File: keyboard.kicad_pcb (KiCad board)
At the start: 2 copper layers, 74 parts, among them CON1 USB-MICRO-B, J1 CONN-PALM-FOLD-KB, P1 Keyboard Even, P2 Keyboard Odd, P3 PS2, P4 Palm Serial, P5 ARM debug header, Q1 BSS138, Q2 BSS138, Q3 BSS138, SW1 SW_PUSH, U1 CONN-X220-KB, U2 MCP1700-2202E/TT, U3 EFM32G222F32, X1 CRYSTAL

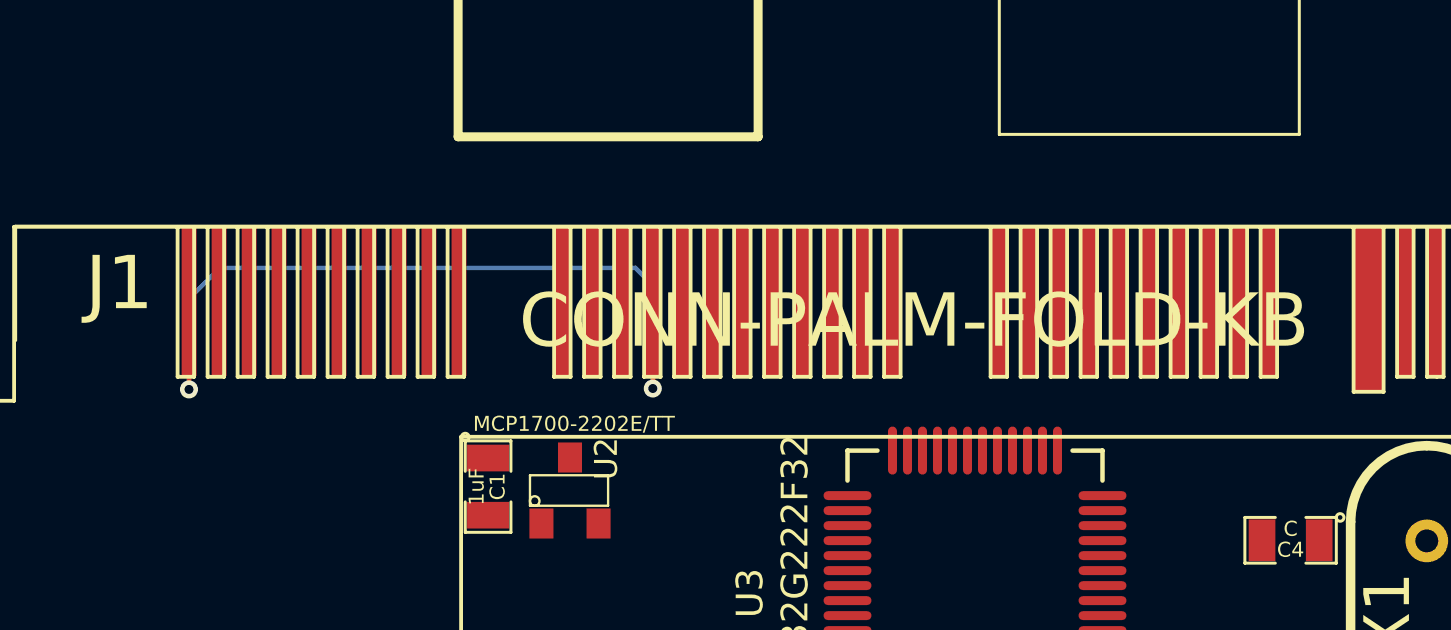
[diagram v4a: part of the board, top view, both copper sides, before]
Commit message: First pass at joining up the duplicated palm connections
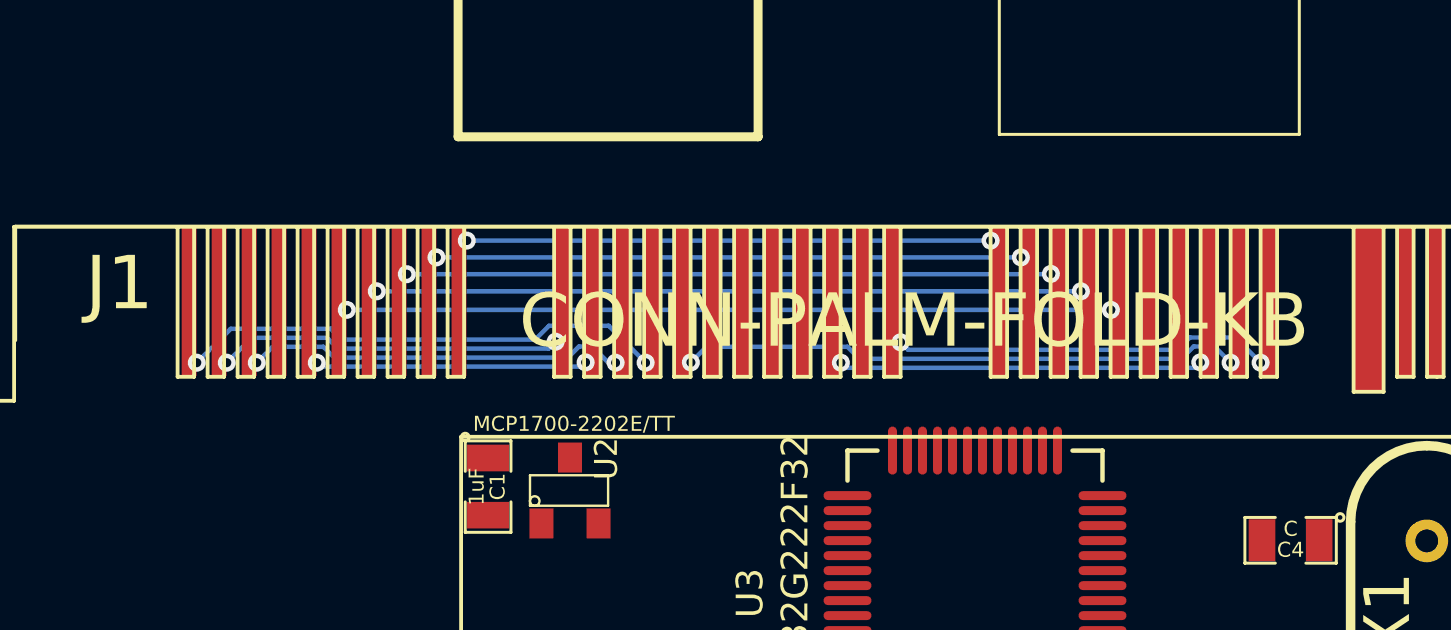
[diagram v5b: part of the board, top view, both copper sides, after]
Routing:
- net row8: track 0.00 -> 26.3 mm, vias 0 -> 2
- net col12: track 0.00 -> 24.3 mm, vias 0 -> 2
- net row7: track 0.00 -> 23.5 mm, vias 0 -> 2
- net col5: track 0.00 -> 23.1 mm, vias 0 -> 2
- net row6: track 0.00 -> 22.6 mm, vias 0 -> 2
- net row5: track 0.00 -> 21.7 mm, vias 0 -> 2
- net col8: track 0.00 -> 17.0 mm, vias 0 -> 2
- net col6: track 0.00 -> 16.4 mm, vias 0 -> 2
- net col1: track 0.00 -> 16.3 mm, vias 0 -> 2
- net col10: track 0.00 -> 15.2 mm, vias 0 -> 2
- net col9: track 0.00 -> 13.4 mm, vias 0 -> 2
- net col7: track 28.5 -> 20.6 mm

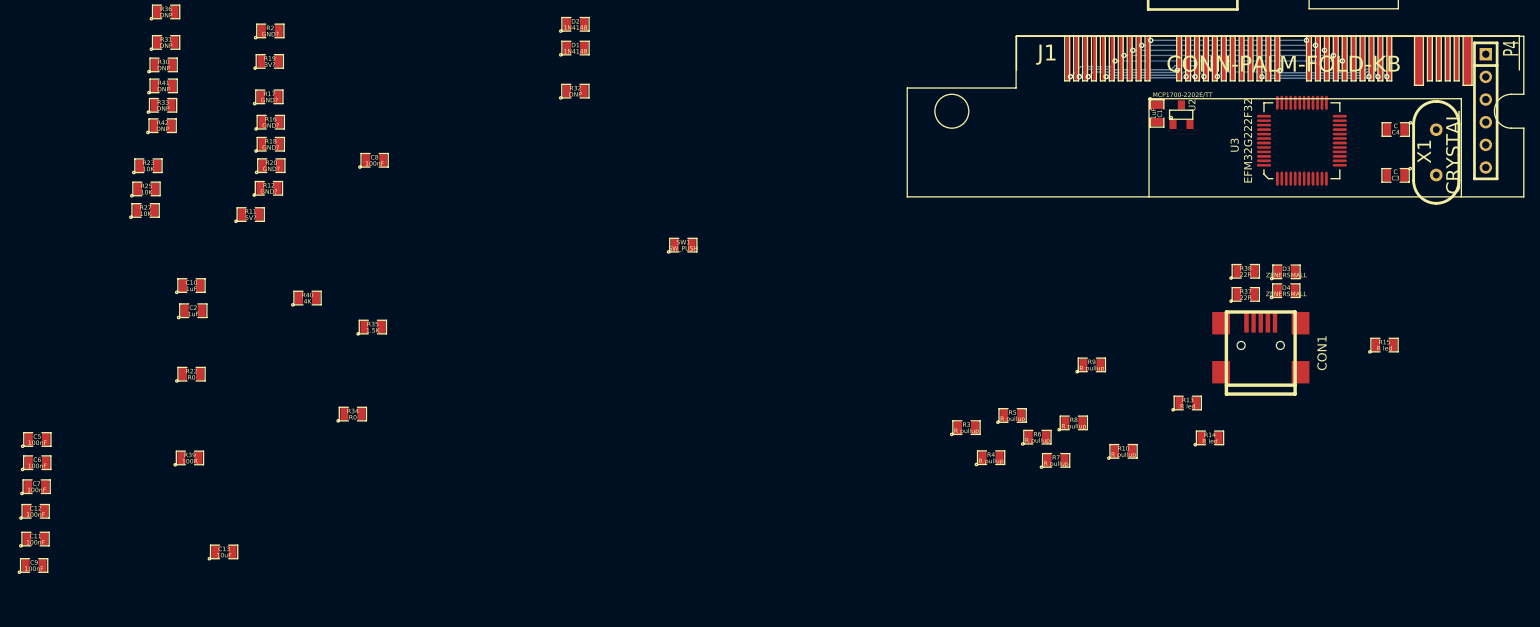
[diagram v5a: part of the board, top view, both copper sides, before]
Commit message: Route most of the palm board, ensuring that there was also enough escape for the rest of the board
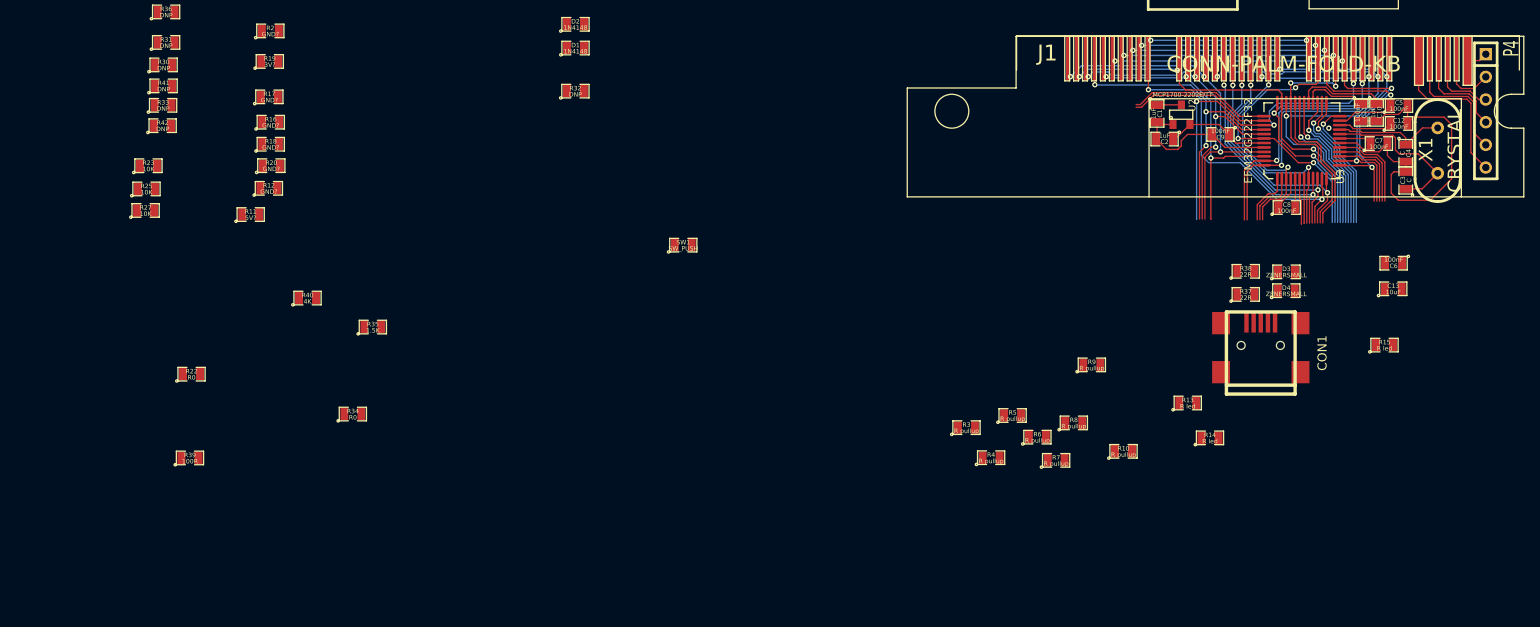
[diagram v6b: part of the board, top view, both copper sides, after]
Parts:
- moved C12 158.9 mm to (185.1, 52.8)
- moved C5 157.1 mm to (185.1, 50.8)
- moved C11 156.1 mm to (180.9, 51.5), turned to 270 degrees
- moved C7 155.3 mm to (182.9, 55.0)
- moved C6 153.6 mm to (184.5, 68.4), turned to 180 degrees
- moved C9 141.5 mm to (165.1, 54.0), turned to 180 degrees
- moved C13 134.3 mm to (184.5, 71.3)
- moved C10 134.2 mm to (182.6, 51.5), turned to 270 degrees
- moved C2 110.5 mm to (158.8, 54.5), turned to 180 degrees
- moved C8 102.4 mm to (172.5, 62.2)
- moved C4 2.88 mm to (185.9, 56.1), turned to 270 degrees
- moved C3 1.27 mm to (185.9, 59.1), turned to 90 degrees
- moved X1 0.26 mm to (189.4, 55.8)
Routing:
- net GND: track 0.00 -> 63.8 mm
- net col11: track 0.00 -> 39.3 mm, vias 0 -> 3
- net +3.3V: track 0.00 -> 39.2 mm
- net row5: track 21.7 -> 58.8 mm, vias 2 -> 4
- net col3: track 0.00 -> 37.1 mm, vias 0 -> 3
- net col10: track 15.2 -> 48.2 mm, vias 2 -> 3
- net col2: track 0.00 -> 32.8 mm, vias 0 -> 3
- net col1: track 16.3 -> 47.0 mm, vias 2 -> 3
- net row6: track 22.6 -> 52.8 mm, vias 2 -> 4
- net col5: track 23.1 -> 51.9 mm, vias 2 -> 3
- net row2: track 0.00 -> 28.6 mm, vias 0 -> 2
- net row7: track 23.5 -> 52.0 mm, vias 2 -> 4
- net col6: track 16.4 -> 44.7 mm, vias 2 -> 3
- net col12: track 24.3 -> 52.0 mm, vias 2 -> 4
- net col4: track 0.00 -> 27.6 mm, vias 0 -> 3
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
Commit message: Fully routed board, done with new kicad 5533
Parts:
- removed CON1: USB-MICRO-B, USB_MINI_B
- added P6: Power, Pin_Headers:Pin_Header_Straight_1x04, F.Cu at (132.7, 96.8)
- added P7: USB_H, Pin_Headers:Pin_Header_Straight_1x04, F.Cu at (140.6, 81.7)
- added REF**: DNP, Resistors_SMD:R_0805_HandSoldering, F.Cu at (196.3, 105.3)
- added USB: USB-MICRO-B, USB_MINI_B, F.Cu at (134.2, 86.5)
- R30, R31: footprint SM0805 -> Resistors_SMD:R_0805
- moved R27 151.7 mm to (196.2, 68.3)
- moved R23 147.8 mm to (192.3, 68.3)
- moved R25 143.7 mm to (188.2, 68.3)
- moved R2 137.8 mm to (189.8, 84.6)
- moved R12 134.4 mm to (189.8, 88.6)
- moved R20 134.3 mm to (189.8, 86.6)
- moved R31 133.7 mm to (163.9, 108.4), turned to 90 degrees
- moved R19 132.3 mm to (183.2, 90.3)
- moved R11 132.0 mm to (186.3, 86.6)
- moved R30 131.2 mm to (163.9, 105.2), turned to 90 degrees
- moved R18 124.5 mm to (178.2, 90.1)
- moved R36 122.0 mm to (167.0, 62.0)
- moved R22 121.1 mm to (168.2, 106.2), turned to 180 degrees
- moved R17 120.0 mm to (175.8, 75.3)
- moved R16 119.6 mm to (175.7, 77.1)
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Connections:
- C11 pad 1: +3.3V -> +3V3
- C12 pad 1: +3.3V -> +3V3
- C13 pad 1: +3.3V -> +3V3
- C2 pad 1: +3.3V -> +3V3
- C5 pad 1: +3.3V -> +3V3
- C7 pad 1: +3.3V -> +3V3
- C8 pad 1: +3.3V -> +3V3
- C9 pad 1: +3.3V -> +3V3
- D2 pad 2: +5V -> +3V3
- P3 pad 2: (no net) -> Net-(P3-Pad2)
- P5 pad 1: +3.3V -> +3V3
- P5 pad 11: (no net) -> Net-(P5-Pad11)
- P5 pad 13: (no net) -> Net-(P5-Pad13)
- P5 pad 17: (no net) -> Net-(P5-Pad17)
- P5 pad 19: (no net) -> Net-(P5-Pad19)
- P5 pad 2: (no net) -> Net-(P5-Pad2)
- P5 pad 3: (no net) -> Net-(P5-Pad3)
- P5 pad 5: (no net) -> Net-(P5-Pad5)
- Q1 pad 1: +3.3V -> +3V3
- Q2 pad 1: +3.3V -> +3V3
- Q3 pad 1: +3.3V -> +3V3
- R1 pad 1: (no net) -> ledmicmute
- R10 pad 1: +3.3V -> +3V3
- R19 pad 1: +3.3V -> +3V3
- R21 pad 2: +3.3V -> +3V3
- R24 pad 2: +3.3V -> +3V3
- R26 pad 2: +3.3V -> +3V3
- R3 pad 1: +3.3V -> +3V3
- R33 pad 2: +3.3V -> +3V3
- R36 pad 2: +3.3V -> +3V3
- R4 pad 1: +3.3V -> +3V3
- R40 pad 2: +3.3V -> +3V3
- R5 pad 1: +3.3V -> +3V3
- R6 pad 1: +3.3V -> +3V3
- R7 pad 1: +3.3V -> +3V3
- R8 pad 1: +3.3V -> +3V3
- R9 pad 1: +3.3V -> +3V3
- U2 pad 2: +3.3V -> +3V3
- U3 pad 19: +3.3V -> +3V3
- U3 pad 22: +3.3V -> +3V3
- U3 pad 23: +3.3V -> +3V3
- U3 pad 28: +3.3V -> +3V3
- U3 pad 4: +3.3V -> +3V3
- U3 pad 43: +3.3V -> +3V3
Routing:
- net GND: track 63.8 -> 648.6 mm, vias 0 -> 60
- net +3V3: track 0.00 -> 255.3 mm, vias 0 -> 10
- net +5V: track 0.00 -> 164.7 mm, vias 0 -> 6
- net pwrswitch: track 0.00 -> 120.9 mm, vias 0 -> 2
- net Net-(P2-Pad13): track 0.00 -> 112.2 mm, vias 0 -> 4
- net row6: track 52.8 -> 151.6 mm
- net hotkey: track 6.31 -> 102.8 mm
- net row1: track 26.5 -> 122.1 mm
- net row8: track 52.9 -> 144.5 mm
- net row4: track 27.0 -> 114.4 mm, vias 2 -> 4
- net row3: track 27.2 -> 112.7 mm, vias 2 -> 4
- net row5: track 58.8 -> 142.7 mm, vias 4 -> 6
- net row2: track 28.6 -> 109.8 mm, vias 2 -> 4
- net Net-(P2-Pad12): track 0.00 -> 78.3 mm, vias 0 -> 2
- net col3: track 37.1 -> 114.9 mm, vias 3 -> 4
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- added copper zone on B.Cu, net GND
- added copper zone on F.Cu, net GND
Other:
- board outline added: 69.1 x 68.1 mm
- net class Pwr added: clearance 0.2, trace_width 0.2, via_dia 0.65, via_drill 0.35
- board text added: "1"
- board text added: "10"
- board text added: "15"
- board text added: "2"
- board text added: "20"
- board text added: "25"
- board text added: "30"
- board text added: "35"
- board text added: "40"
- board text added: "5"
- board text added: "Keyboard v1"

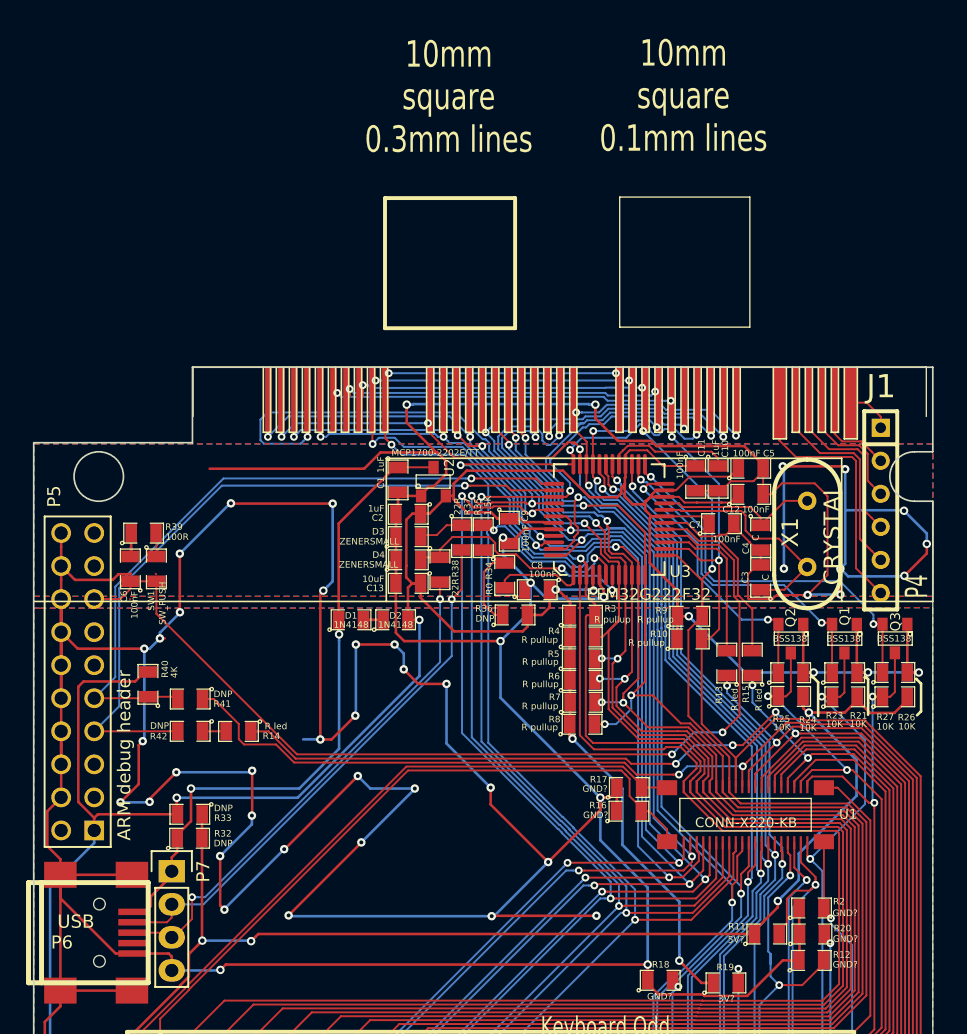
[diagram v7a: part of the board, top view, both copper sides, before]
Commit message: Tidy up silkscreen and one gnd plane misplaced via
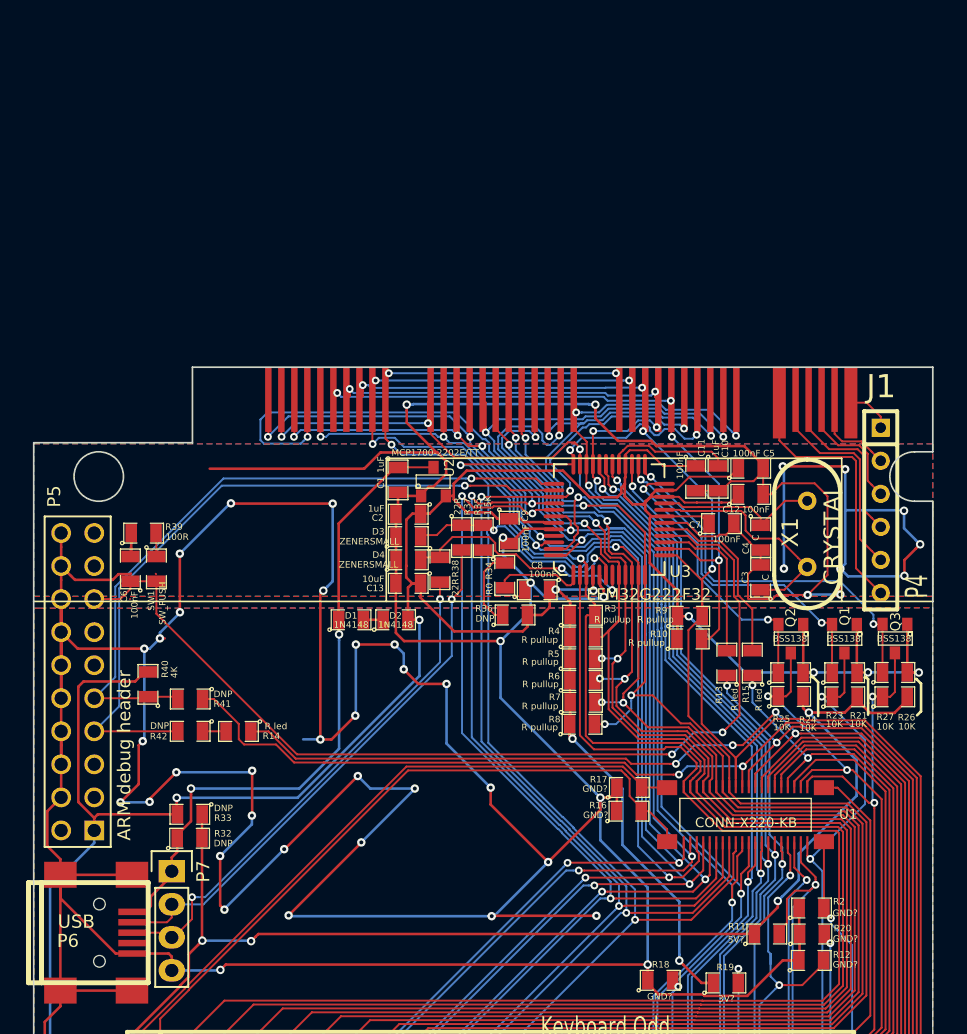
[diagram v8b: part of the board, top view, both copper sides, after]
